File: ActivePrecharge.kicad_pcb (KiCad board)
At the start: 2 copper layers, 69.5 x 61.5 mm, 66 parts, among them Con1 LED, IC1 1769205241, J1 Conn_01x03, J2 Conn_01x02, J3 Conn_01x02, Q1 PMV35EPER, Q2 IRLML0030, Q2 PMV35EPER, Q3 IRLML0030, U1 NCP785AH50T1G, U1I_TP1 TestPoint, U2 NCP785AH50T1G, U2I_TP1 TestPoint, U2O_TP1 TestPoint, U3 TLV9301xDCK, U4 TCMT1106

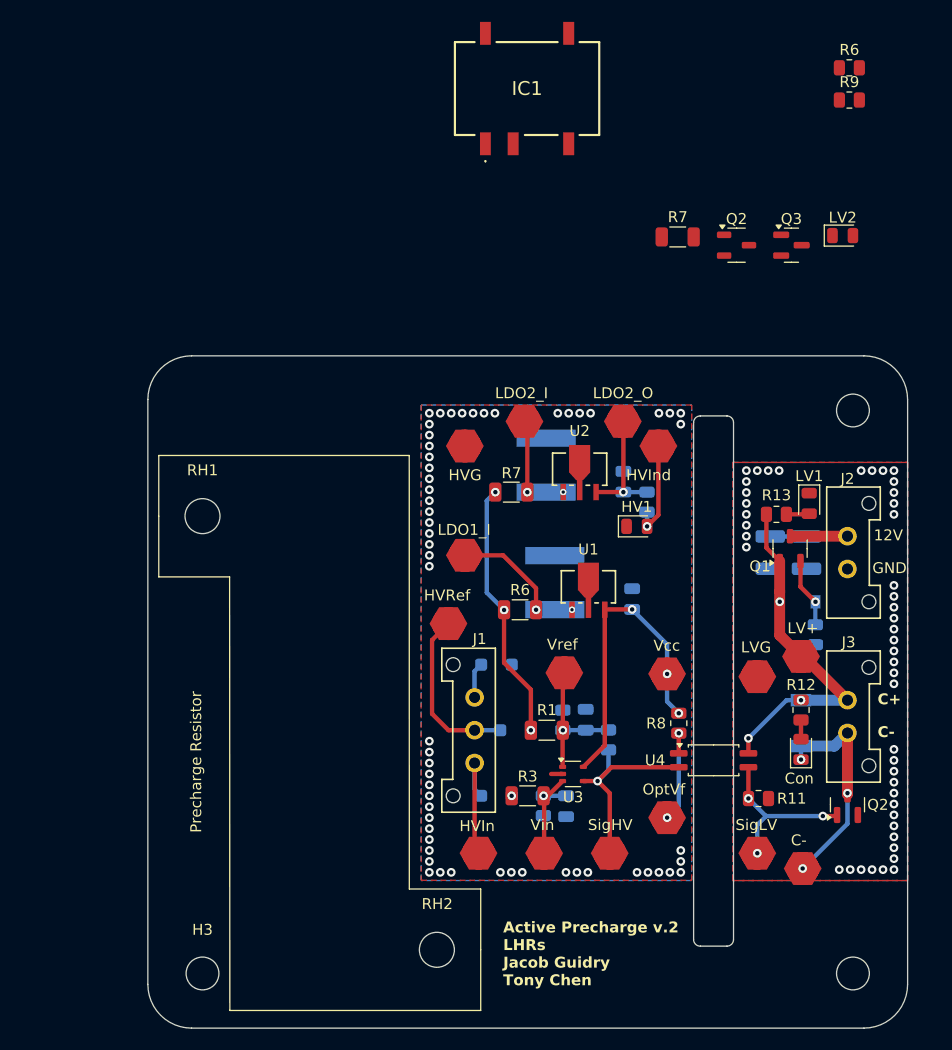
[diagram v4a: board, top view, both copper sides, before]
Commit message: layout and sch ready for review (isolated DCDC convertor version)
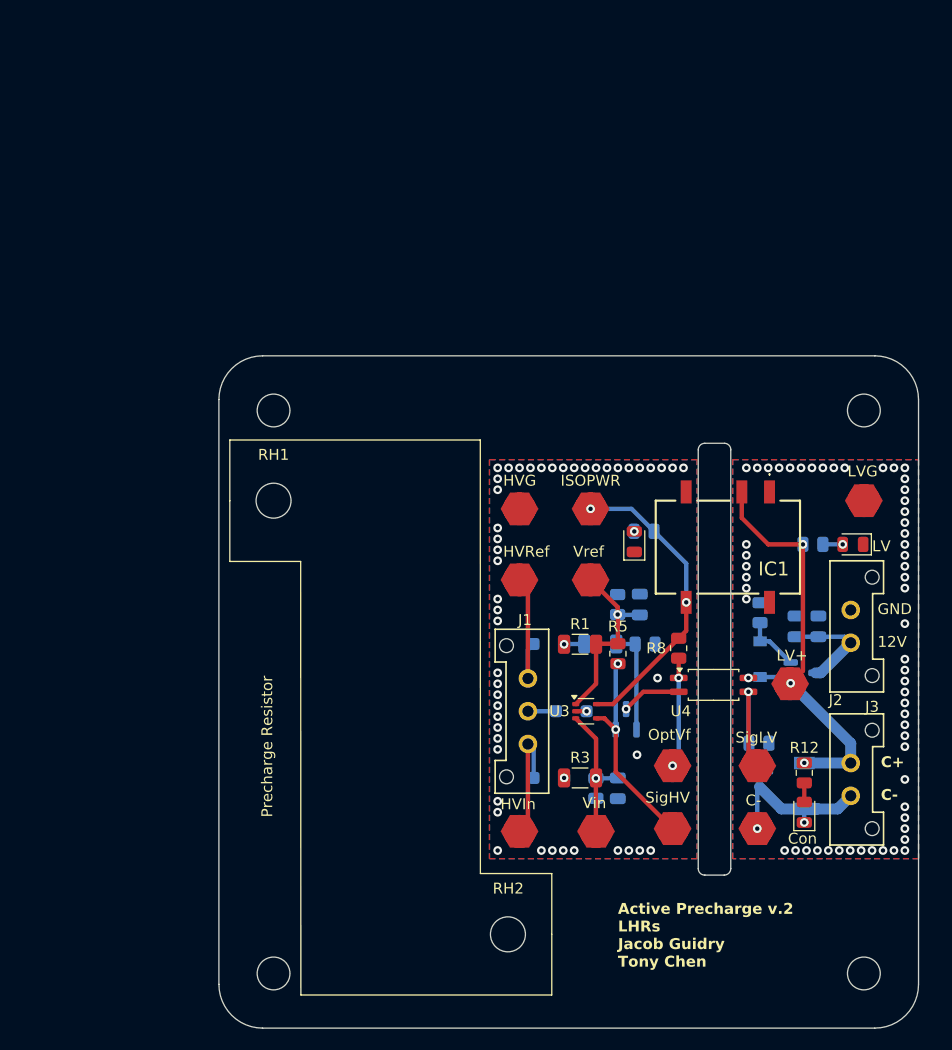
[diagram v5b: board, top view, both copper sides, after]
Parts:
- removed the C3 at (112.7, 88.2)
- removed the C4 at (119.8, 89.8)
- removed C5: 2.2u, Active-PrechargeLib:CAPC5750X220N
- removed C6: 22u, Capacitor_SMD:C_0805_2012Metric
- removed the HV1 at (120.2, 83.1)
- removed HVI_TP2, U1I_TP1, U2I_TP1, U2O_TP1, Vcc_TP1: TestPoint, Active-PrechargeLib:TestPoint_HEX_3mmID
- removed the Q2 at (139.5, 108.6)
- removed the Q2 at (129.4, 57.4)
- removed the R6 at (109.5, 90.7)
- removed the R7 at (108.8, 80.0)
- removed the R9 at (121.2, 80.9)
- removed U1, U2: NCP785AH50T1G, Active-PrechargeLib:SOT-89-3_2P7X4P7_ONS
- added H4: MountingHole, MountingHole:MountingHole_3mm, F.Cu at (87.0, 72.5)
- added ISO_PWR_TP1: TestPoint, Active-PrechargeLib:TestPoint_HEX_3mmID, F.Cu at (116.0, 81.5)
- added Q3: IRLML0030, Package_TO_SOT_SMD:SOT-23, B.Cu at (131.4, 106.0)
- C3: renamed from C7; footprint Capacitor_SMD:C_1210_3225Metric -> Capacitor_SMD:C_0805_2012Metric
- C4: renamed from C8; footprint Capacitor_SMD:C_1210_3225Metric -> Capacitor_SMD:C_0805_2012Metric
- Q1: renamed from Q3; moved to B.Cu
- Q2: renamed from Q1; moved to B.Cu
- R11, R13, R9: moved to B.Cu
- R5: moved to F.Cu
- R6: renamed from R7; moved to B.Cu
- R7: renamed from R6; moved to B.Cu
- moved R7 55.9 mm to (121.0, 93.9)
- moved Q1 45.9 mm to (119.2, 100.8), turned to 90 degrees
- moved IC1 45.8 mm to (128.6, 85.0), turned to 180 degrees
- moved R9 43.7 mm to (120.9, 83.5), turned to 180 degrees
- moved R6 37.9 mm to (116.9, 93.9)
- moved HV1 33.9 mm to (120.0, 84.5), turned to 90 degrees
- moved LVGND_TP1 18.8 mm to (141.0, 80.8)
- moved R2 11.7 mm to (118.5, 90.2)
- moved C1 11.6 mm to (120.5, 90.2)
- moved Q2 11.4 mm to (135.4, 96.5), turned to 0 degrees
- moved Ref_TP1 8.83 mm to (116.0, 88.0)
- moved D2 8.46 mm to (112.2, 93.9)
- moved R1 8.43 mm to (115.0, 93.9)
- moved D1 8.07 mm to (114.2, 100.0)
- moved SigLV_TP1 8.00 mm to (131.2, 105.0)
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- renumbered LV2 to HV1
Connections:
- Con-_TP1 pad 1: Net-(D5-K) -> Net-(Con1-K)
- Con1 pad 1: GND -> Net-(Con1-K)
- D5 pad 1: Net-(D5-K) -> /LV+
- D5 pad 2: GND -> Net-(Con1-K)
- IC1 pad 5: /Vcc+ -> /ISO_PWR
- J1 pad 2: HRef -> HGND
- J1 pad 3: HGND -> HRef
- J2 pad 1: +12V -> LVGND
- J2 pad 2: LVGND -> +12V
- J3 pad 1: Net-(D5-K) -> /LV+
- J3 pad 2: GND -> Net-(Con1-K)
- Q1 pad 2: /SignalHV -> Net-(Q1-S)
- Q1 pad 3: Net-(Q3-D) -> /SignalHV
- R12 pad 2: Net-(D5-K) -> /LV+
- R5 pad 2: Net-(Q3-D) -> Net-(Q1-S)
- R8 pad 1: Net-(OptVf_TP1-Pad1) -> /ISO_PWR
- R8 pad 2: /SignalHV -> Net-(OptVf_TP1-Pad1)
- R9 pad 1: /Vcc+ -> /ISO_PWR
- SigHV_TP1 pad 1: Net-(Q3-D) -> Net-(Q1-S)
- U3 pad 2: HGND -> /HVGND
- U3 pad 4: Net-(Q3-D) -> Net-(Q1-S)
- U3 pad 5: /Vcc+ -> /ISO_PWR
- U4 pad 2: /HVGND -> /SignalHV
- U4 pad 4: +12V -> /LV+
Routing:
- net /LV+: track 0.00 -> 40.1 mm, vias 0 -> 4
- net +12V: track 44.1 -> 9.64 mm, vias 3 -> 0
- net /Vcc+: track 29.0 -> 0.00 mm, vias 3 -> 0
- net /ISO_PWR: track 0.00 -> 28.0 mm, vias 0 -> 2
- net /HRef: track 23.8 -> 0.00 mm, vias 3 -> 0
- net Net-(Q1-S): track 0.00 -> 19.5 mm, vias 0 -> 2
- net /SignalHV: track 19.6 -> 5.47 mm
- net Net-(U2-VOUT): track 11.1 -> 0.00 mm, vias 1 -> 0
- net Net-(U1-VIN): track 9.73 -> 0.00 mm, vias 2 -> 0
- net Net-(Q1-G): track 0.00 -> 9.59 mm
- net Net-(HV1-A) (its old number): track 9.09 -> 0.00 mm, vias 1 -> 0
- net Net-(U2-VIN): track 6.58 -> 0.00 mm, vias 2 -> 0
- net Net-(U3-+): track 12.9 -> 17.2 mm
- net Net-(Con1-K): track 20.2 -> 16.0 mm, vias 3 -> 2
- net /Vin: track 9.62 -> 13.1 mm
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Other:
- board size 69.5 x 61.5 mm -> 64 x 61.5 mm
- board text added: "ISOPWR"
- board text added: "J2"
- board text added: "LV"
- board text removed: "HVInd"
- board text removed: "LDO1_I"
- board text removed: "LDO2_I"
- board text removed: "LDO2_O"
- board text removed: "Vcc"

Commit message: added silkscreen labels to HV 1x3 connector
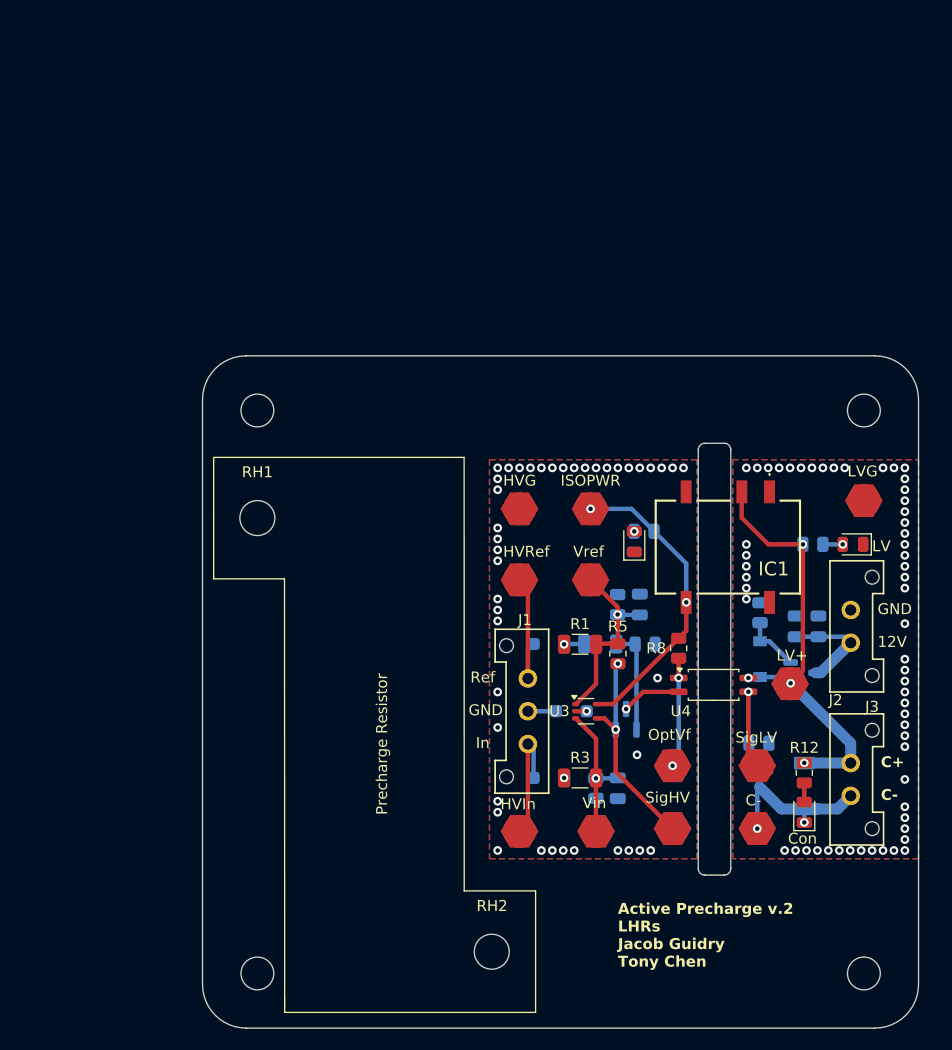
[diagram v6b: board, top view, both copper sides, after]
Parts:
- moved RH1 2.17 mm to (85.5, 82.3)
- moved RH2 2.17 mm to (107.0, 122.0)
- moved H3 1.48 mm to (85.5, 124.0)
- moved H4 1.48 mm to (85.5, 72.5)
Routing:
- net /HVGND: vias 49 -> 43
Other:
- board size 64 x 61.5 mm -> 65.5 x 61.5 mm
- board text added: "In"
- board text added: "Ref"

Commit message: finished for review
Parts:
- moved C1 2.13 mm to (118.5, 89.5)
- moved R2 2.13 mm to (116.5, 89.5)
- moved R7 0.11 mm to (121.1, 93.9), turned to 180 degrees
- moved R6 0.08 mm to (116.8, 93.9)
- turned R5 to 90 degrees
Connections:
- C1 pad 1: Net-(U3-+) -> /Vref
- R1 pad 2: Net-(U3-+) -> /Vref
- R2 pad 1: Net-(U3-+) -> /Vref
- R5 pad 1: Net-(U3-+) -> Net-(Q1-S)
- R5 pad 2: Net-(Q1-S) -> /Vref
- R7 pad 1: Net-(Q1-G) -> /HVGND
- R7 pad 2: /HVGND -> Net-(Q1-G)
- Ref_TP1 pad 1: Net-(U3-+) -> /Vref
- U3 pad 1: Net-(U3-+) -> /Vref
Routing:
- net Net-(U3-+): track 17.2 -> 0.00 mm, vias 1 -> 0
- net /Vref: track 0.00 -> 17.2 mm, vias 0 -> 1
- net LVGND: track 0.00 -> 2.80 mm, vias 57 -> 55
- net /LV+: track 40.1 -> 41.1 mm

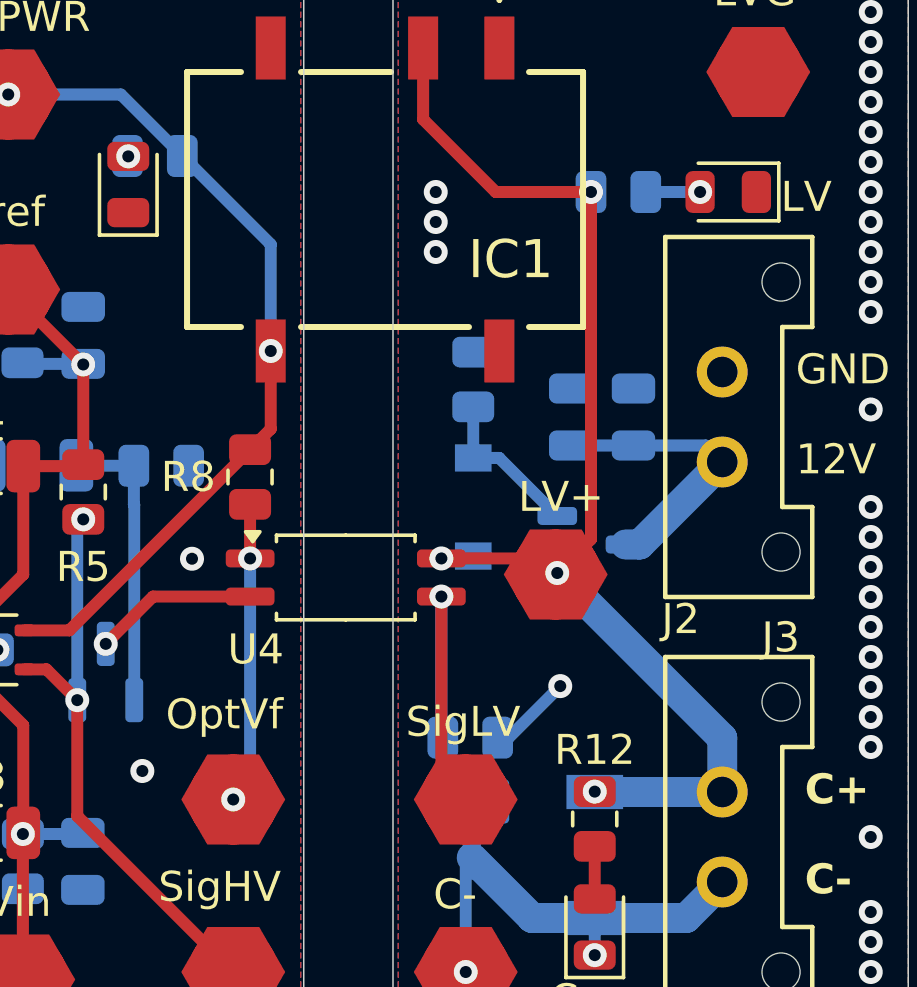
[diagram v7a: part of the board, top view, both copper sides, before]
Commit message: fixed incorrect pmos pinout
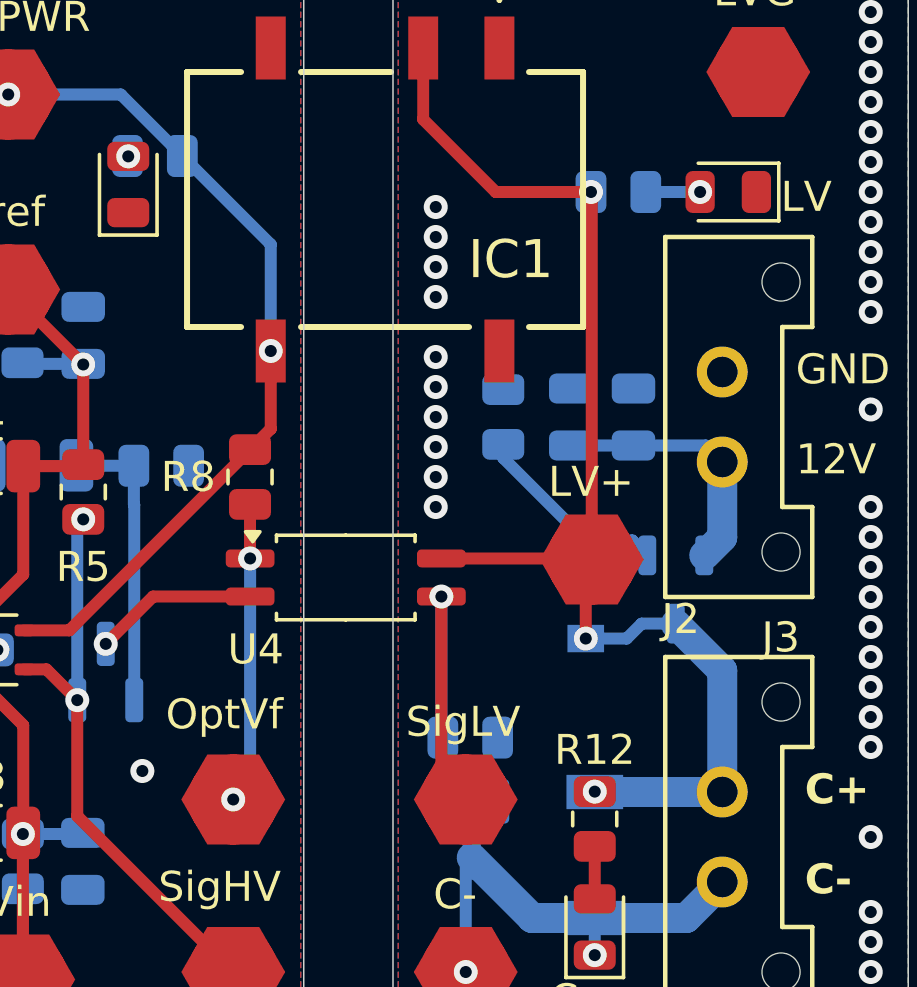
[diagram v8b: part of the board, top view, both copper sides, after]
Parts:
- removed Q2: PMV35EPER, Package_TO_SOT_SMD:SOT-23-3
- added Q4: Q_PMOS_GDS, Package_TO_SOT_SMD:SOT-23-3, B.Cu at (138.2, 98.0)
- 12V_TP1, Con-_TP1, HVG_TP1, HVI_TP1, HVR_TP1, IN_TP1, ISO_PWR_TP1, LVGND_TP1, OptVf_TP1, Ref_TP1, SigHV_TP1, SigLV_TP1: footprint Active-PrechargeLib:TestPoint_HEX_3mmID -> utsvt-special:TestPoint_HEX_3mmID
- moved D4 4.65 mm to (135.2, 98.0)
- moved R10 1.60 mm to (132.5, 92.2)
- moved 12V_TP1 1.30 mm to (135.4, 97.0)
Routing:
- net LVGND: track 2.80 -> 0.00 mm, vias 55 -> 61
- net /LV+: track 41.1 -> 42.7 mm, vias 4 -> 3
- net Net-(D4-A): track 5.30 -> 6.60 mm
- net +12V: track 9.64 -> 8.64 mm
- net /HVGND: vias 43 -> 42
